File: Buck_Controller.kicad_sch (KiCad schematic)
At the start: 10 parts, among them U1 LM25085MM, U2 LM25085MM

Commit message: ALCUNE MODIFICHE AL CIRCUITO
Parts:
- added Cbyp1, Cbyp2: C, symbol Device:C
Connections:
- net GND: now also Cbyp1.2, Cbyp2.2
- net Vin: now also Cbyp1.1, Cbyp2.1
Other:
- moved on the sheet: RT
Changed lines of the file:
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@@
   (junction (at 137.795 38.735) (diameter 0) (color 0 0 0 0)
   )
+  (junction (at 124.46 72.39) (diameter 0) (color 0 0 0 0)
+  )
   (junction (at 107.315 106.68) (diameter 0) (color 0 0 0 0)
   )
+  (junction (at 99.06 51.435) (diameter 0) (color 0 0 0 0)
+  )
   (junction (at 157.48 56.515) (diameter 0) (color 0 0 0 0)
   )
@@
   (junction (at 156.845 111.76) (diameter 0) (color 0 0 0 0)
   )
+  (junction (at 96.52 106.68) (diameter 0) (color 0 0 0 0)
+  )
+  (junction (at 123.825 128.27) (diameter 0) (color 0 0 0 0)
+  )
   (junction (at 175.26 104.14) (diameter 0) (color 0 0 0 0)
   )
-  (wire (pts (xy 107.95 51.435) (xy 107.95 54.61))
+  (wire (pts (xy 107.95 51.435) (xy 107.95 53.975))
     (stroke (width 0) (type default) (color 0 0 0 0))
   )
@@
     (stroke (width 0) (type default) (color 0 0 0 0))
   )
-  (wire (pts (xy 107.95 64.135) (xy 107.95 62.23))
+  (wire (pts (xy 107.95 64.135) (xy 107.95 61.595))
     (stroke (width 0) (type default) (color 0 0 0 0))
   )
@@
     (stroke (width 0) (type default) (color 0 0 0 0))
   )
+  (wire (pts (xy 96.52 106.68) (xy 107.315 106.68))
+    (stroke (width 0) (type default) (color 0 0 0 0))
+  )
   (wire (pts (xy 137.795 95.885) (xy 137.795 97.79))
     (stroke (width 0) (type default) (color 0 0 0 0))
@@
     (stroke (width 0) (type default) (color 0 0 0 0))
   )
-  (wire (pts (xy 88.265 51.435) (xy 107.95 51.435))
+  (wire (pts (xy 88.265 51.435) (xy 99.06 51.435))
     (stroke (width 0) (type default) (color 0 0 0 0))
   )
@@
     (stroke (width 0) (type default) (color 0 0 0 0))
   )
-  (wire (pts (xy 87.63 106.68) (xy 107.315 106.68))
+  (wire (pts (xy 87.63 106.68) (xy 96.52 106.68))
     (stroke (width 0) (type default) (color 0 0 0 0))
   )
@@
     (stroke (width 0) (type default) (color 0 0 0 0))
   )
-  (wire (pts (xy 124.46 71.755) (xy 124.46 74.295))
+  (wire (pts (xy 124.46 71.755) (xy 124.46 72.39))
+    (stroke (width 0) (type default) (color 0 0 0 0))
+  )
+  (wire (pts (xy 124.46 72.39) (xy 124.46 74.295))
+    (stroke (width 0) (type default) (color 0 0 0 0))
+  )
+  (wire (pts (xy 99.06 51.435) (xy 107.95 51.435))
     (stroke (width 0) (type default) (color 0 0 0 0))
   )
@@
     (stroke (width 0) (type default) (color 0 0 0 0))
   )
+  (wire (pts (xy 99.06 61.595) (xy 99.06 72.39))
+    (stroke (width 0) (type default) (color 0 0 0 0))
+  )
   (polyline (pts (xy 76.2 146.05) (xy 76.2 89.535))
     (stroke (width 0) (type default) (color 0 0 0 0))
@@
     (stroke (width 0) (type default) (color 0 0 0 0))
   )
+  (wire (pts (xy 96.52 106.68) (xy 96.52 110.49))
+    (stroke (width 0) (type default) (color 0 0 0 0))
+  )
+  (wire (pts (xy 96.52 118.11) (xy 96.52 128.27))
+    (stroke (width 0) (type default) (color 0 0 0 0))
+  )
   (wire (pts (xy 157.48 56.515) (xy 163.195 56.515))
     (stroke (width 0) (type default) (color 0 0 0 0))
@@
     (stroke (width 0) (type default) (color 0 0 0 0))
   )
+  (wire (pts (xy 99.06 72.39) (xy 124.46 72.39))
+    (stroke (width 0) (type default) (color 0 0 0 0))
+  )
   (wire (pts (xy 134.62 51.435) (xy 137.795 51.435))
     (stroke (width 0) (type default) (color 0 0 0 0))
@@
     (stroke (width 0) (type default) (color 0 0 0 0))
   )
+  (wire (pts (xy 123.825 128.27) (xy 123.825 129.54))
+    (stroke (width 0) (type default) (color 0 0 0 0))
+  )
   (wire (pts (xy 137.795 42.545) (xy 137.795 38.735))
     (stroke (width 0) (type default) (color 0 0 0 0))
@@
     (stroke (width 0) (type default) (color 0 0 0 0))
   )
-  (wire (pts (xy 123.825 127) (xy 123.825 129.54))
+  (wire (pts (xy 123.825 127) (xy 123.825 128.27))
     (stroke (width 0) (type default) (color 0 0 0 0))
   )
@@
     (stroke (width 0) (type default) (color 0 0 0 0))
   )
+  (wire (pts (xy 99.06 51.435) (xy 99.06 53.975))
+    (stroke (width 0) (type default) (color 0 0 0 0))
+  )
   (wire (pts (xy 175.26 104.14) (xy 175.26 111.76))
+    (stroke (width 0) (type default) (color 0 0 0 0))
+  )
+  (wire (pts (xy 96.52 128.27) (xy 123.825 128.27))
     (stroke (width 0) (type default) (color 0 0 0 0))
   )
@@
     (pin "2")
   )
-  (symbol (lib_id "Device:R") (at 107.95 58.42 0) (unit 1)
-    (in_bom yes) (on_board yes) (fields_autoplaced)
-    (property "Reference" "RT" (id 0) (at 110.49 57.1499 0)
-      (effects (font (size 1.27 1.27)) (justify left))
-    )
-    (property "Value" "R" (id 1) (at 110.49 59.6899 0)
-      (effects (font (size 1.27 1.27)) (justify left))
-    )
-    (property "Footprint" "" (id 2) (at 106.172 58.42 90)
-      (effects (font (size 1.27 1.27)) hide)
-    )
-    (property "Datasheet" "~" (id 3) (at 107.95 58.42 0)
+  (symbol (lib_id "Device:R") (at 107.95 57.785 0) (unit 1)
+    (in_bom yes) (on_board yes) (fields_autoplaced)
+    (property "Reference" "RT" (id 0) (at 110.49 56.5149 0)
+      (effects (font (size 1.27 1.27)) (justify left))
+    )
+    (property "Value" "R" (id 1) (at 110.49 59.0549 0)
+      (effects (font (size 1.27 1.27)) (justify left))
+    )
+    (property "Footprint" "" (id 2) (at 106.172 57.785 90)
+      (effects (font (size 1.27 1.27)) hide)
+    )
+    (property "Datasheet" "~" (id 3) (at 107.95 57.785 0)
       (effects (font (size 1.27 1.27)) hide)
     )
@@
       (effects (font (size 1.27 1.27)) hide)
     )
+    (pin "1")
+    (pin "2")
+  )
+  (symbol (lib_id "Device:C") (at 99.06 57.785 0) (unit 1)
+    (in_bom yes) (on_board yes)
+    (property "Reference" "Cbyp1" (id 0) (at 90.805 56.515 0)
+      (effects (font (size 1.27 1.27)) (justify left))
+    )
+    (property "Value" "C" (id 1) (at 90.805 59.055 0)
+      (effects (font (size 1.27 1.27)) (justify left))
+    )
+    (property "Footprint" "" (id 2) (at 100.0252 61.595 0)
+      (effects (font (size 1.27 1.27)) hide)
+    )
+    (property "Datasheet" "~" (id 3) (at 99.06 57.785 0)
+      (effects (font (size 1.27 1.27)) hide)
+    )
+    (pin "1")
+    (pin "2")
+  )
+  (symbol (lib_id "Device:C") (at 96.52 114.3 0) (unit 1)
+    (in_bom yes) (on_board yes)
+    (property "Reference" "Cbyp2" (id 0) (at 87.63 112.395 0)
+      (effects (font (size 1.27 1.27)) (justify left))
+    )
+    (property "Value" "C" (id 1) (at 87.63 114.935 0)
+      (effects (font (size 1.27 1.27)) (justify left))
+    )
+    (property "Footprint" "" (id 2) (at 97.4852 118.11 0)
+      (effects (font (size 1.27 1.27)) hide)
+    )
+    (property "Datasheet" "~" (id 3) (at 96.52 114.3 0)
+      (effects (font (size 1.27 1.27)) hide)
+    )

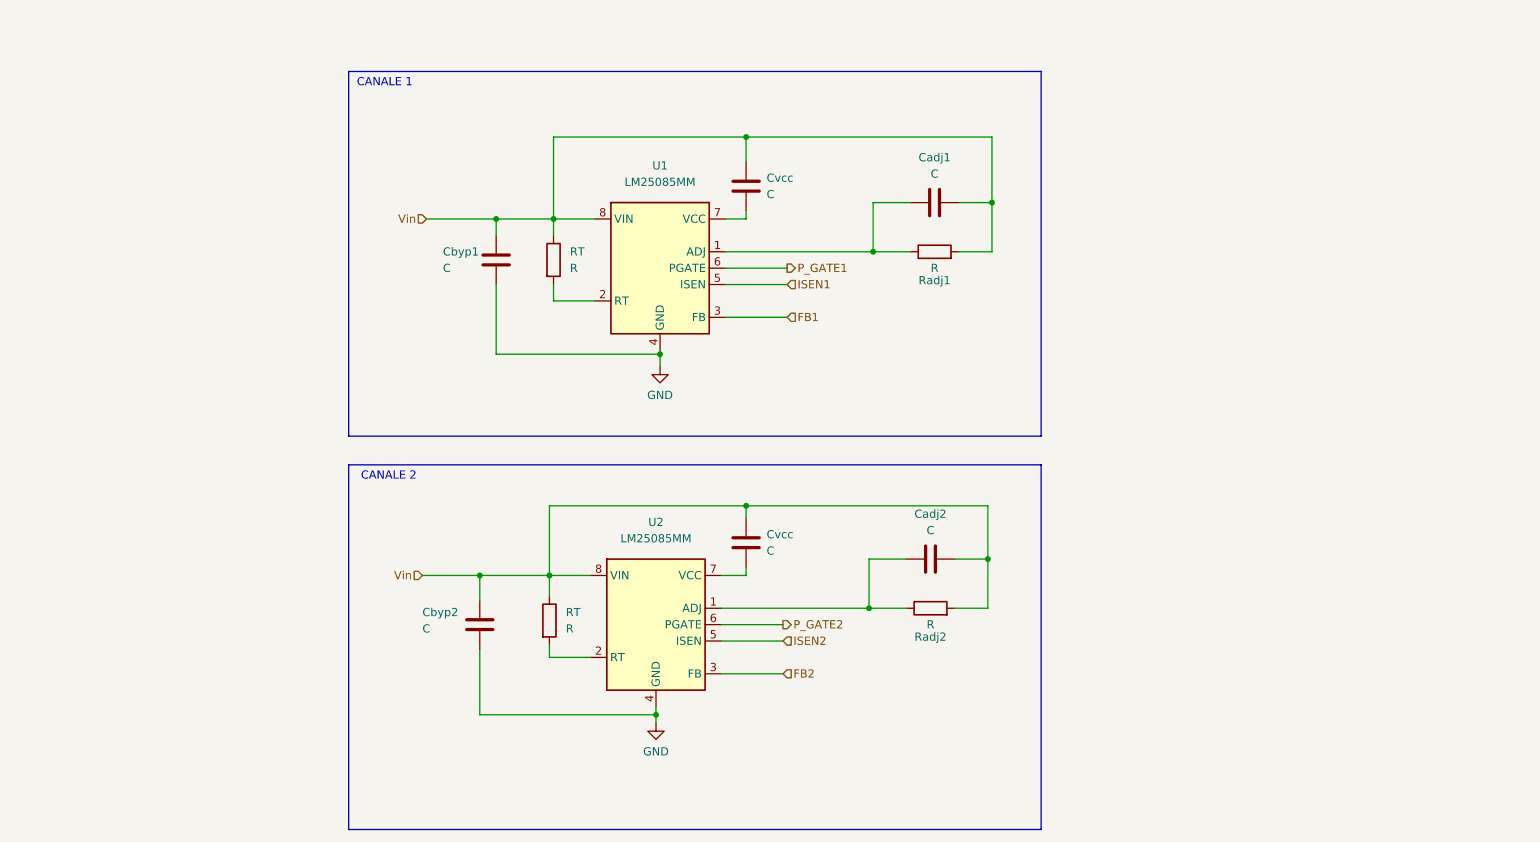
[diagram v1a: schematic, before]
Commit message: aggiunta di un file che esplicita alcuni calcoli
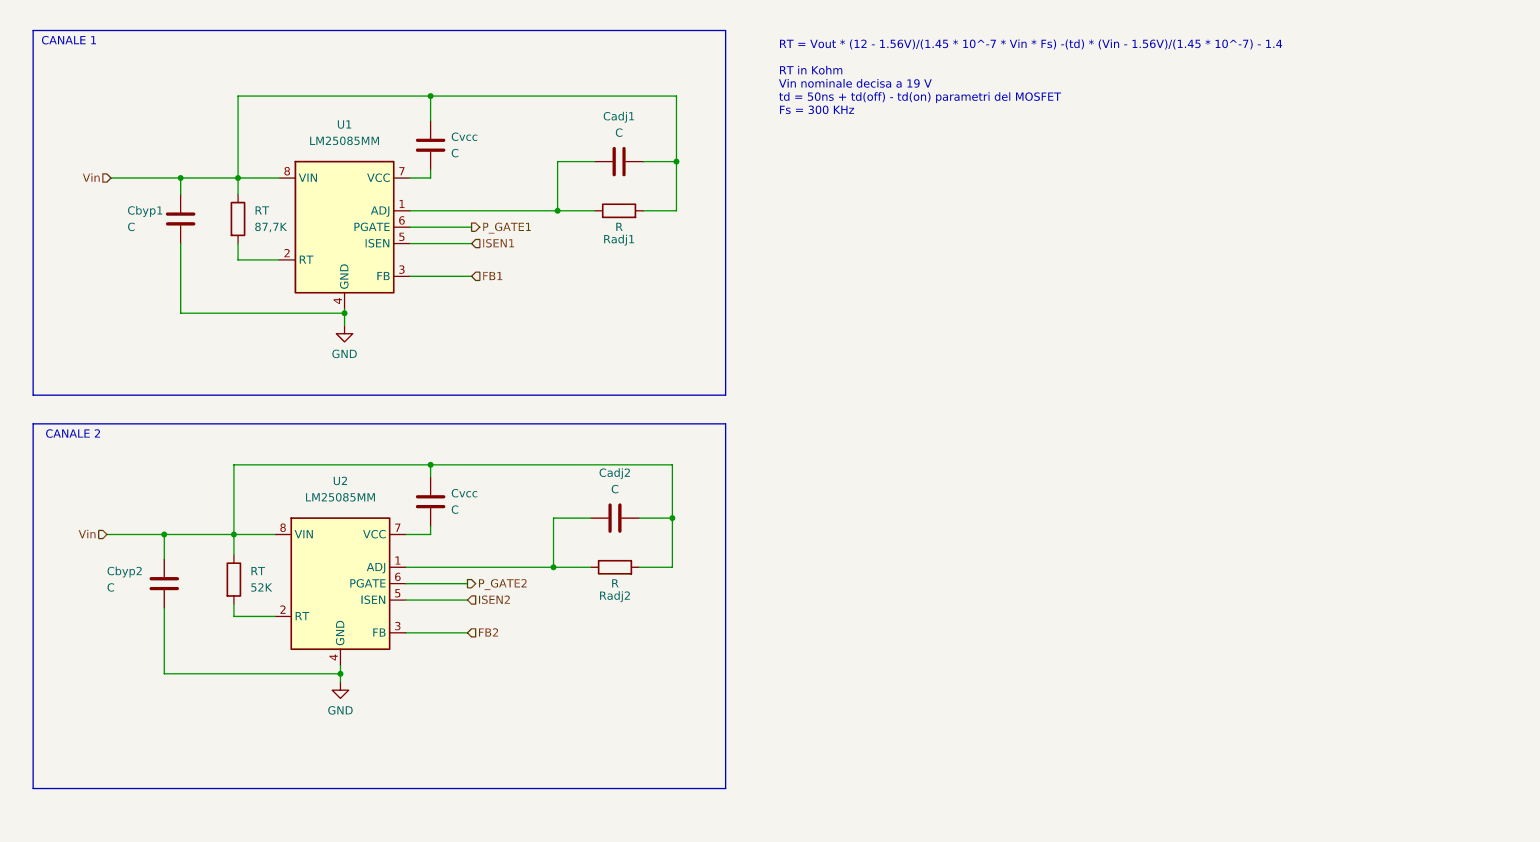
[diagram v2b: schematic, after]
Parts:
- RT: value R -> 52K
- RT: value R -> 87,7K
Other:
- note added: "RT = Vout * (12 - 1.56V)/(1.45 * 10^-7 * Vin * Fs) -(td) * (Vin - 1.56V)/(1.45 * 10^-7) - 1.4 RT in Kohm Vin nominale decisa a 19 V td = 50ns + td(off) - td(on) parametri del MOSFET Fs = 300 KHz"
- moved on the sheet: Cadj1, Cadj2, Cbyp1, Cbyp2, Cvcc, RT, Radj1, Radj2, U1, U2

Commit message: aggiornato il foglio di calcolo per il dimensionamento dell'alimentatore
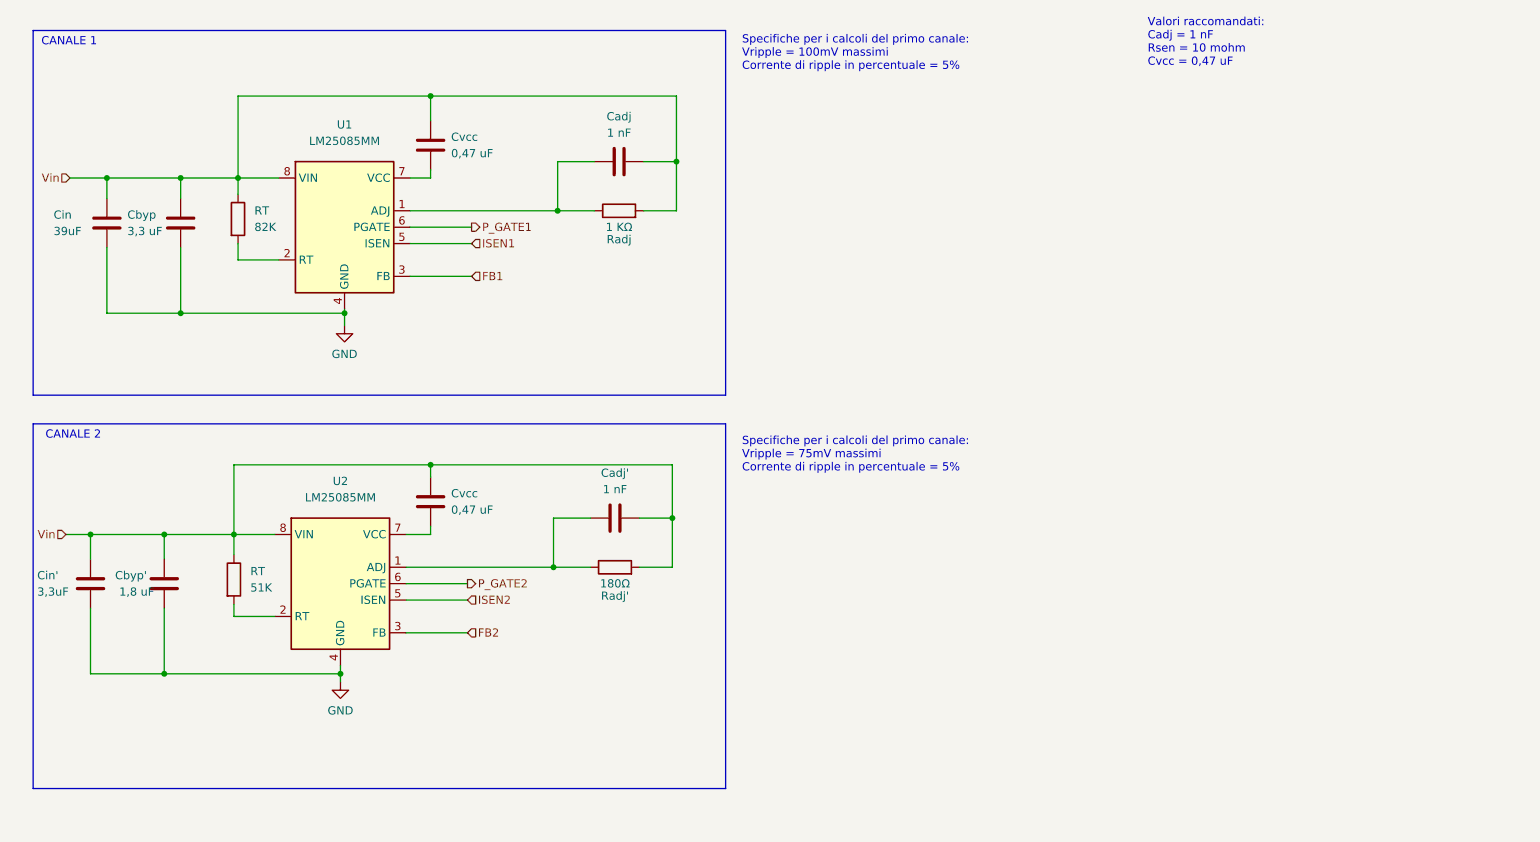
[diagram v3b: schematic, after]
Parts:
- added Cin: 39uF, symbol Device:C
- added Cin': 3,3uF, symbol Device:C
- Cadj: renamed from Cadj1; value C -> 1 nF
- Cadj': renamed from Cadj2; value C -> 1 nF
- Cbyp: renamed from Cbyp1; value C -> 3,3 uF
- Cbyp': renamed from Cbyp2; value C -> 1,8 uF
- Cvcc: value C -> 0,47 uF
- RT: value 52K -> 51K
- RT: value 87,7K -> 82K
- Radj: renamed from Radj1; value R -> 1 KΩ
- Radj': renamed from Radj2; value R -> 180Ω
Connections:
- net GND: now also Cin'.2, Cin.2
- net Vin: now also Cin'.1, Cin.1
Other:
- note added: "Specifiche per i calcoli del primo canale: Vripple = 100mV massimi Corrente di ripple in percentuale = 5%"
- note added: "Specifiche per i calcoli del primo canale: Vripple = 75mV massimi Corrente di ripple in percentuale = 5%"
- note added: "Valori raccomandati: Cadj = 1 nF Rsen = 10 mohm Cvcc = 0,47 uF"
- note removed: "RT = Vout * (12 - 1.56V)/(1.45 * 10^-7 * Vin * Fs) -(td) * (Vin - 1.56V)/(1.45 * 10^-7) - 1.4 RT in Kohm Vin nominale decisa a 19 V td = 50ns + td(off) - td(on) parametri del MOSFET Fs = 300 KHz"
- moved on the sheet: Cbyp

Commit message: alcune modifiche ai package di alcuni componenti e continuazione del design del circuito stampato
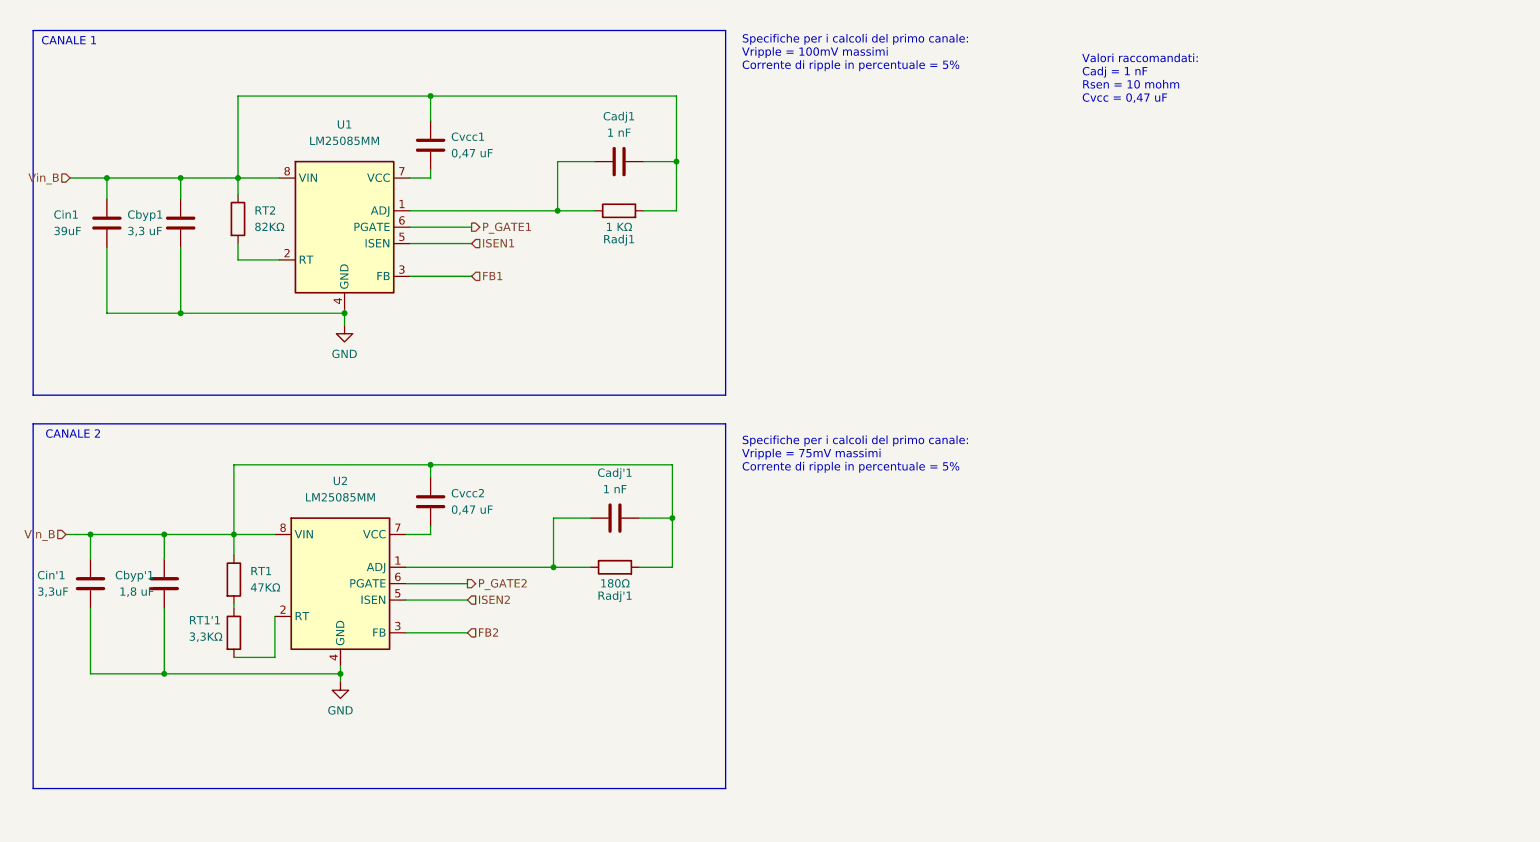
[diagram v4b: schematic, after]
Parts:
- added RT1'1: 3,3KΩ, Resistor_SMD:R_0402_1005Metric, symbol Device:R
- Cadj'1: renamed from Cadj'; footprint (none) -> Capacitor_SMD:C_0402_1005Metric
- Cadj1: renamed from Cadj; footprint (none) -> Capacitor_SMD:C_0402_1005Metric
- Cbyp'1: renamed from Cbyp'; footprint (none) -> Capacitor_SMD:C_0603_1608Metric
- Cbyp1: renamed from Cbyp; footprint (none) -> Capacitor_SMD:C_0603_1608Metric
- Cin'1: renamed from Cin'; footprint (none) -> Capacitor_SMD:C_0603_1608Metric
- Cin1: renamed from Cin; footprint (none) -> Capacitor_SMD:C_0603_1608Metric
- Cvcc1, Cvcc2: renamed from Cvcc; footprint (none) -> Capacitor_SMD:C_0402_1005Metric
- RT1: renamed from RT; value 51K -> 47KΩ; footprint (none) -> Resistor_SMD:R_0402_1005Metric
- RT2: renamed from RT; value 82K -> 82KΩ; footprint (none) -> Resistor_SMD:R_0603_1608Metric
- Radj'1: renamed from Radj'; footprint (none) -> Resistor_SMD:R_0402_1005Metric
- Radj1: renamed from Radj; footprint (none) -> Resistor_SMD:R_0603_1608Metric
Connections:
- net at RT1.2: now also RT1'1.1; no longer U2.2 (RT)
- net Vin renamed Vin_B
- new net: RT1'1.2, U2.2 (RT)
